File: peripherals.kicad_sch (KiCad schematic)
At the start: 11 parts, among them J10 PinHeader_2x5_P2.54mm_SMD, J11 PinHeader_2x5_P2.54mm_SMD, J12 PinHeader_2x5_P2.54mm_SMD, J13 PinHeader_2x5_P2.54mm_SMD, J17 PinHeader_2x5_P2.54mm_SMD, J3 PinHeader_2x5_P2.54mm_SMD, J4 PinHeader_2x5_P2.54mm_SMD, J5 PinHeader_2x5_P2.54mm_SMD, J6 PinHeader_2x5_P2.54mm_SMD, J7 PinHeader_2x5_P2.54mm_SMD, J9 PinHeader_2x5_P2.54mm_SMD

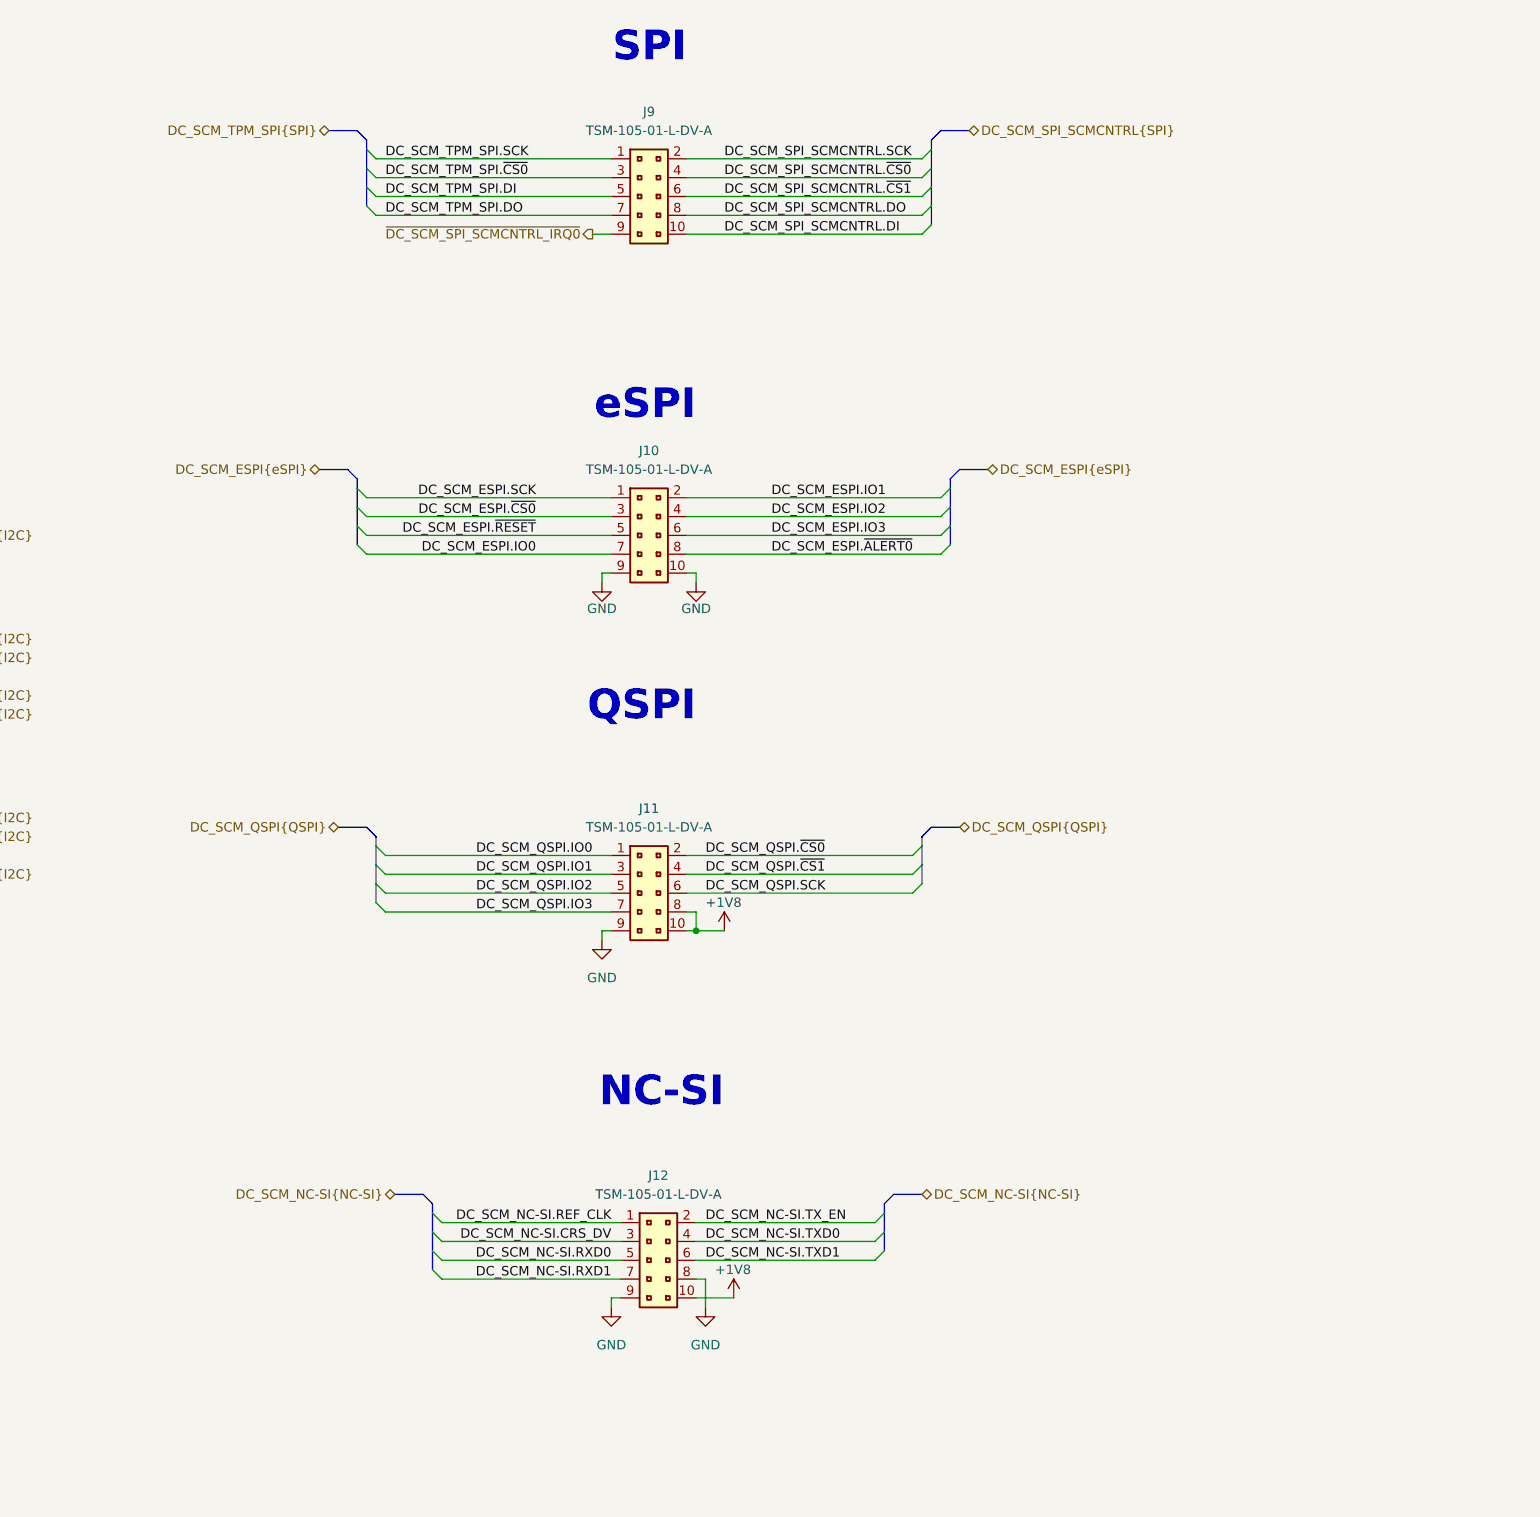
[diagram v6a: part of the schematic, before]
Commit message: [#100720] Finish schematic after PCIe to USB addition
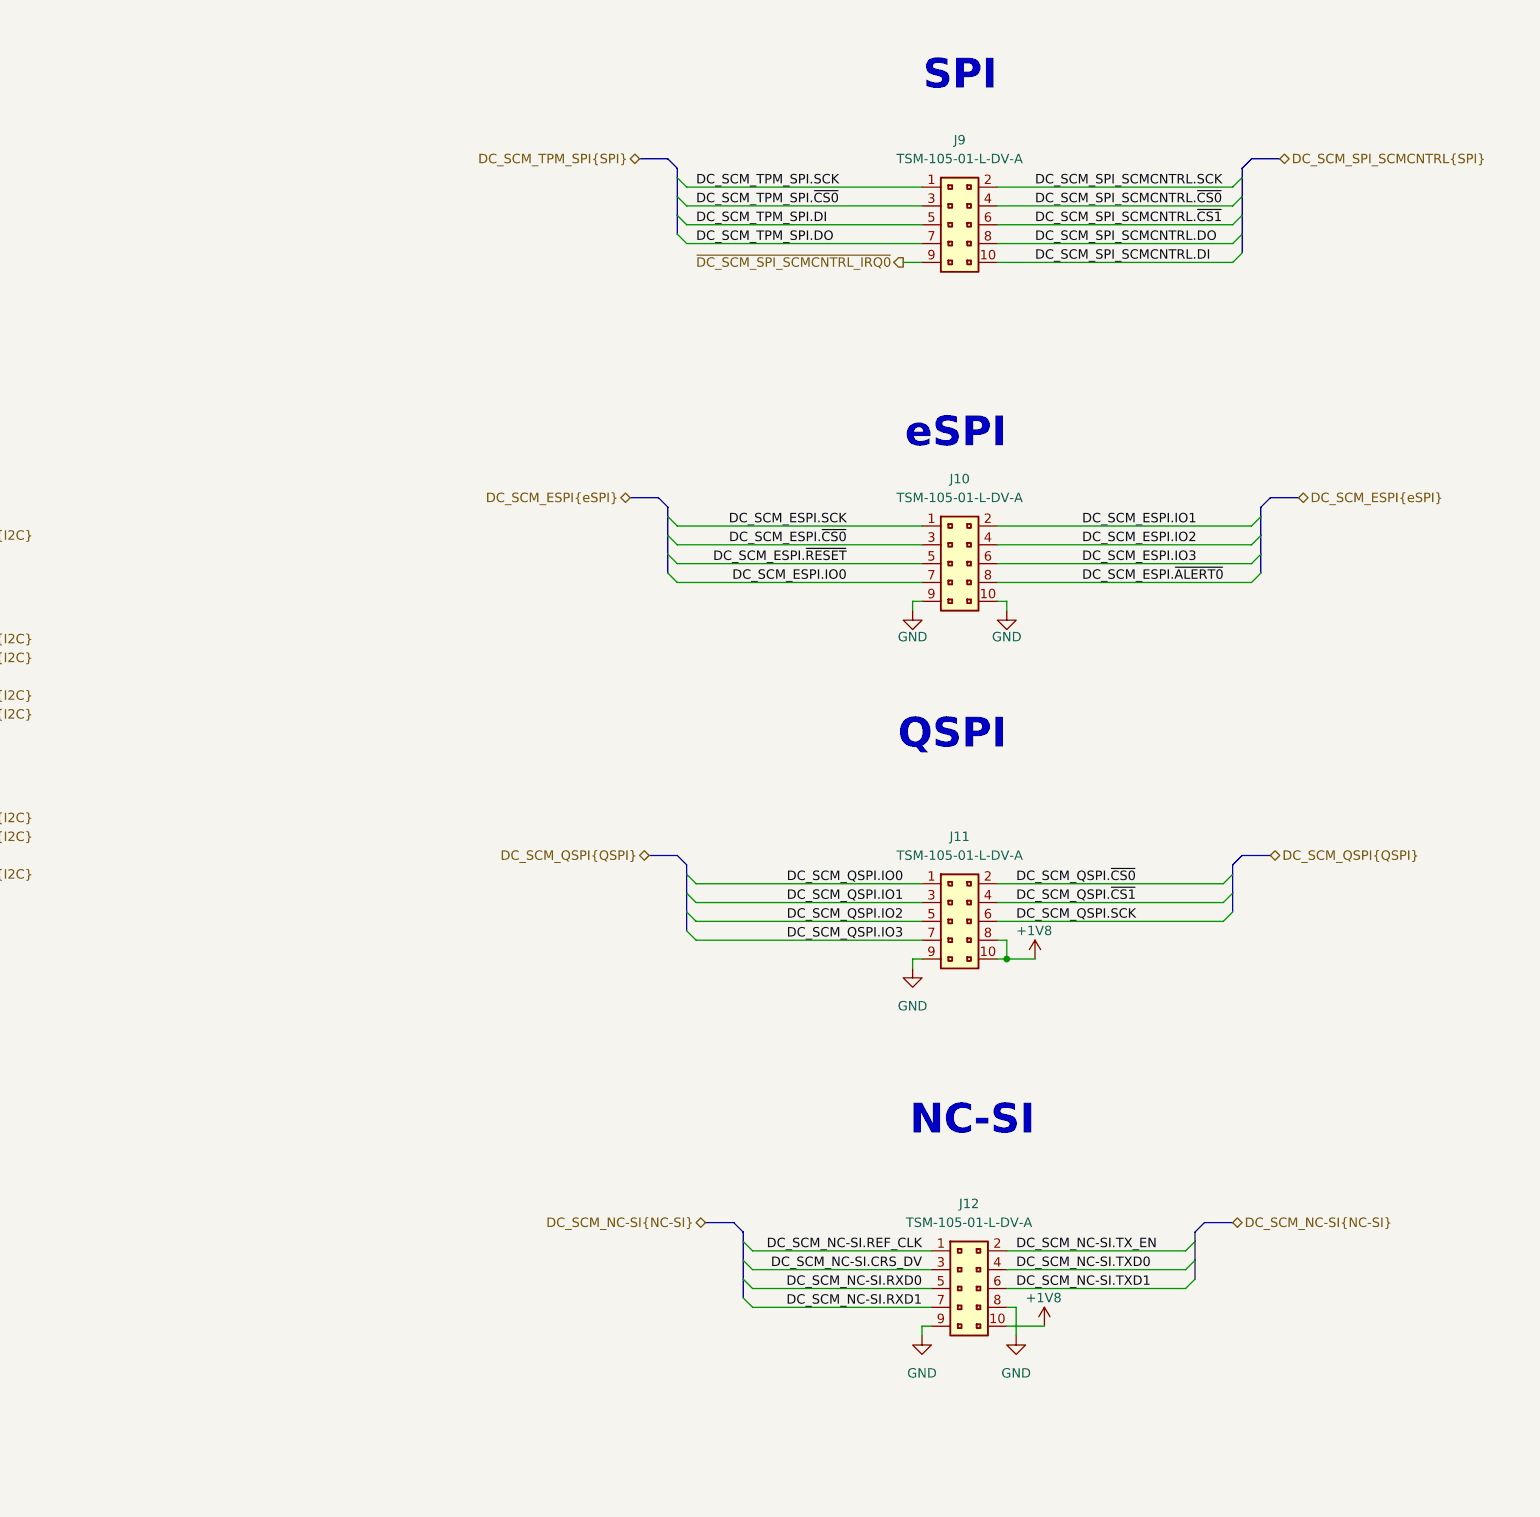
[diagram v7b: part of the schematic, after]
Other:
- moved on the sheet: J10, J11, J12, J9
